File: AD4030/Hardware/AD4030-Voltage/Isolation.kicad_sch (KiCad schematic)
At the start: 26 parts, among them J401 Conn_01x08, J402 Conn_01x07, J403 PMOD, J404 PMOD, U401 ADuM260N, U402 ADuM260N

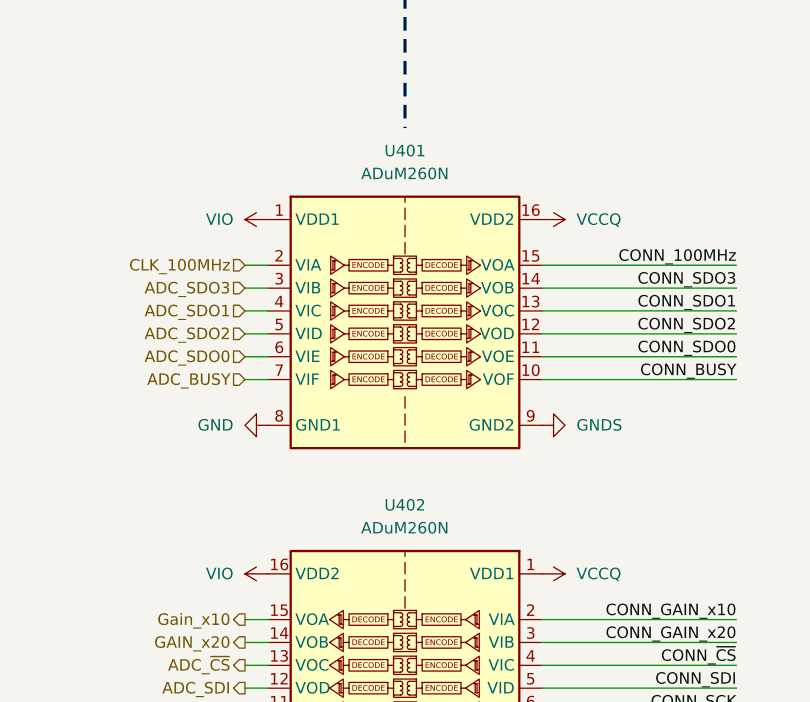
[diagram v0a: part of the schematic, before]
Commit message: AD4030-Voltage : Fixed model names for reference voltage and isolation ICs.
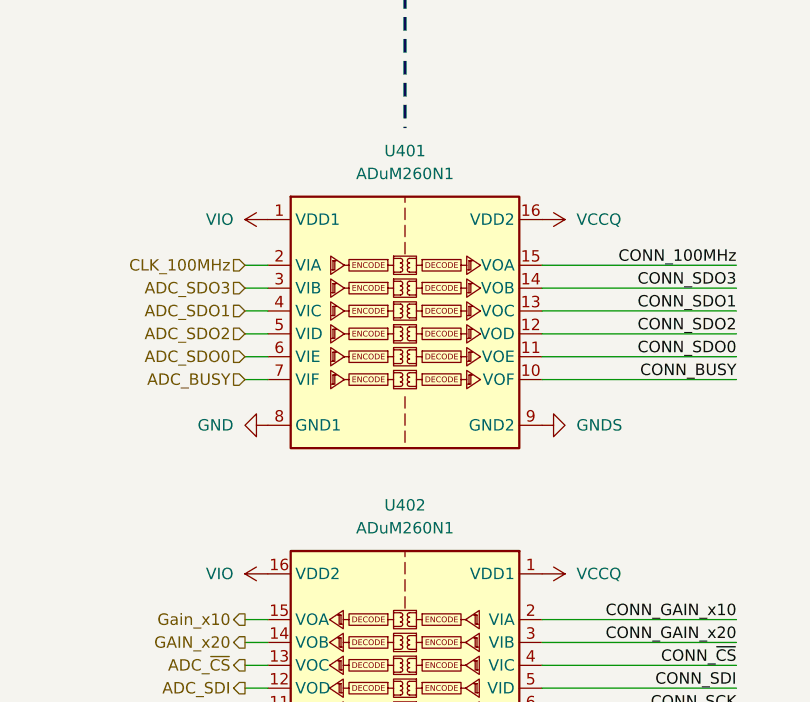
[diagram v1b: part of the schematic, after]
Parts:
- U401, U402: value ADuM260N -> ADuM260N1
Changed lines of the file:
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@@
 			)
 		)
-		(property "Value" "ADuM260N"
+		(property "Value" "ADuM260N1"
 			(at 101.6 53.34 0)
 			(effects
@@
 			)
 		)
-		(property "Value" "ADuM260N"
+		(property "Value" "ADuM260N1"
 			(at 101.6 92.71 0)
 			(effects

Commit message: Development
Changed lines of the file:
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@@
 (kicad_sch
-	(version 20231120)
+	(version 20250114)
 	(generator "eeschema")
-	(generator_version "8.0")
+	(generator_version "9.0")
 	(paper "A4")
 	(junction
@@
 	(label "CONN_GAIN_x10"
 		(at 148.59 115.57 0)
-		(fields_autoplaced yes)
 		(effects
 			(font
@@
 	(label "CONN_SDO1"
 		(at 195.58 66.04 0)
-		(fields_autoplaced yes)
 		(effects
 			(font
@@
 	(label "CONN_GAIN_x20"
 		(at 148.59 113.03 0)
-		(fields_autoplaced yes)
 		(effects
 			(font
@@
 	(label "CONN_BUSY"
 		(at 276.86 63.5 180)
-		(fields_autoplaced yes)
 		(effects
 			(font
@@
 	(label "CONN_~{CS}"
 		(at 148.59 110.49 0)
-		(fields_autoplaced yes)
 		(effects
 			(font
@@
 	(label "CONN_SDO0"
 		(at 195.58 63.5 0)
-		(fields_autoplaced yes)
 		(effects
 			(font
@@
 	(label "CONN_CNV"
 		(at 195.58 93.98 0)
-		(fields_autoplaced yes)
 		(effects
 			(font
@@
 	(label "CONN_GAIN_x20"
 		(at 138.43 105.41 180)
-		(fields_autoplaced yes)
 		(effects
 			(font
@@
 	(label "CONN_SDO1"
 		(at 138.43 68.58 180)
-		(fields_autoplaced yes)
 		(effects
 			(font
@@
 	(label "CONN_GAIN_x10"
 		(at 138.43 102.87 180)
-		(fields_autoplaced yes)
 		(effects
 			(font
@@
 	(label "CONN_SCK"
 		(at 148.59 78.74 0)
-		(fields_autoplaced yes)
 		(effects
 			(font
@@
 	(label "CONN_SDO3"
 		(at 148.59 63.5 0)
-		(fields_autoplaced yes)
 		(effects
 			(font
@@
 	(label "CONN_SDO2"
 		(at 148.59 68.58 0)
-		(fields_autoplaced yes)
 		(effects
 			(font
@@
 	(label "CONN_SDO3"
 		(at 138.43 66.04 180)
-		(fields_autoplaced yes)
 		(effects
 			(font
@@
 	(label "CONN_SDO0"
 		(at 148.59 71.12 0)
-		(fields_autoplaced yes)
 		(effects
 			(font
@@
 	(label "CONN_SDI"
 		(at 195.58 91.44 0)
-		(fields_autoplaced yes)
 		(effects
 			(font
@@
 	(label "CONN_SDO1"
 		(at 148.59 66.04 0)
-		(fields_autoplaced yes)
 		(effects
 			(font
@@
 	(label "CONN_100MHz"
 		(at 195.58 68.58 0)
-		(fields_autoplaced yes)
 		(effects
 			(font
@@
 	(label "CONN_SDO2"
 		(at 276.86 66.04 180)
-		(fields_autoplaced yes)
 		(effects
 			(font
@@
 	(label "CONN_SDO3"
 		(at 276.86 68.58 180)
-		(fields_autoplaced yes)
 		(effects
 			(font
@@
 	(label "CONN_CNV"
 		(at 148.59 76.2 0)
-		(fields_autoplaced yes)
 		(effects
 			(font
@@
 	(label "CONN_100MHz"
 		(at 148.59 60.96 0)
-		(fields_autoplaced yes)
 		(effects
 			(font
@@
 	(label "CONN_SDO0"
 		(at 138.43 73.66 180)
-		(fields_autoplaced yes)
 		(effects
 			(font
@@
 	(label "CONN_CNV"
 		(at 138.43 115.57 180)
-		(fields_autoplaced yes)
 		(effects
 			(font
@@
 	(label "CONN_SDI"
 		(at 138.43 110.49 180)
-		(fields_autoplaced yes)
 		(effects
 			(font
@@
 	(label "CONN_SCK"
 		(at 276.86 93.98 180)
-		(fields_autoplaced yes)
 		(effects
 			(font
@@
 	(label "CONN_~{CS}"
 		(at 276.86 91.44 180)
-		(fields_autoplaced yes)
 		(effects
 			(font
@@
 	(label "CONN_SDI"
 		(at 148.59 107.95 0)
-		(fields_autoplaced yes)
 		(effects
 			(font
@@
 	(label "CONN_SCK"
 		(at 138.43 113.03 180)
-		(fields_autoplaced yes)
 		(effects
 			(font
@@
 	(label "CONN_SDO2"
 		(at 138.43 71.12 180)
-		(fields_autoplaced yes)
 		(effects
 			(font
@@
 	(label "CONN_BUSY"
 		(at 138.43 76.2 180)
-		(fields_autoplaced yes)
 		(effects
 			(font
@@
 	(label "CONN_GAIN_x10"
 		(at 276.86 88.9 180)
-		(fields_autoplaced yes)
 		(effects
 			(font
@@
 	(label "CONN_BUSY"
 		(at 148.59 73.66 0)
-		(fields_autoplaced yes)
 		(effects
 			(font
@@
 	(label "CONN_100MHz"
 		(at 138.43 63.5 180)
-		(fields_autoplaced yes)
 		(effects
 			(font
@@
 	(label "CONN_GAIN_x20"
 		(at 195.58 88.9 0)
-		(fields_autoplaced yes)
 		(effects
 			(font
@@
 	(label "CONN_~{CS}"
 		(at 138.43 107.95 180)
-		(fields_autoplaced yes)
 		(effects
 			(font
@@
 		(shape output)
 		(at 83.82 105.41 180)
-		(fields_autoplaced yes)
 		(effects
 			(font
@@
 		(shape input)
 		(at 83.82 63.5 180)
-		(fields_autoplaced yes)
 		(effects
 			(font
@@
 		(shape input)
 		(at 83.82 73.66 180)
-		(fields_autoplaced yes)
 		(effects
 			(font
@@
 		(shape output)
 		(at 83.82 113.03 180)
-		(fields_autoplaced yes)
 		(effects
 			(font
@@
 		(shape output)
 		(at 83.82 102.87 180)
-		(fields_autoplaced yes)
 		(effects
 			(font
@@
 		(shape input)
 		(at 83.82 66.04 180)
-		(fields_autoplaced yes)
 		(effects
 			(font
@@
 		(shape input)
 		(at 83.82 68.58 180)
-		(fields_autoplaced yes)
 		(effects
 			(font
@@
 		(shape input)
 		(at 83.82 71.12 180)
-		(fields_autoplaced yes)
 		(effects
 			(font
@@
 		(shape output)
 		(at 83.82 107.95 180)
-		(fields_autoplaced yes)
 		(effects
 			(font
@@
 		(shape output)
 		(at 83.82 115.57 180)
-		(fields_autoplaced yes)
 		(effects
 			(font
@@
 		(shape output)
 		(at 83.82 110.49 180)
-		(fields_autoplaced yes)
 		(effects
 			(font
@@
 		(shape input)
 		(at 83.82 76.2 180)
-		(fields_autoplaced yes)
-		(effects
-			(font
+		(effects
+			(font
